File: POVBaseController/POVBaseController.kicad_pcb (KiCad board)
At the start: 2 copper layers, 53.3 x 29.2 mm, 43 parts, among them P1 CONN_01X02, P2 CONN_01X02, P3 CONN_01X05, U1 A5970AD, U2 CY8C4014LQI-412, U3 LD1117S50CTR

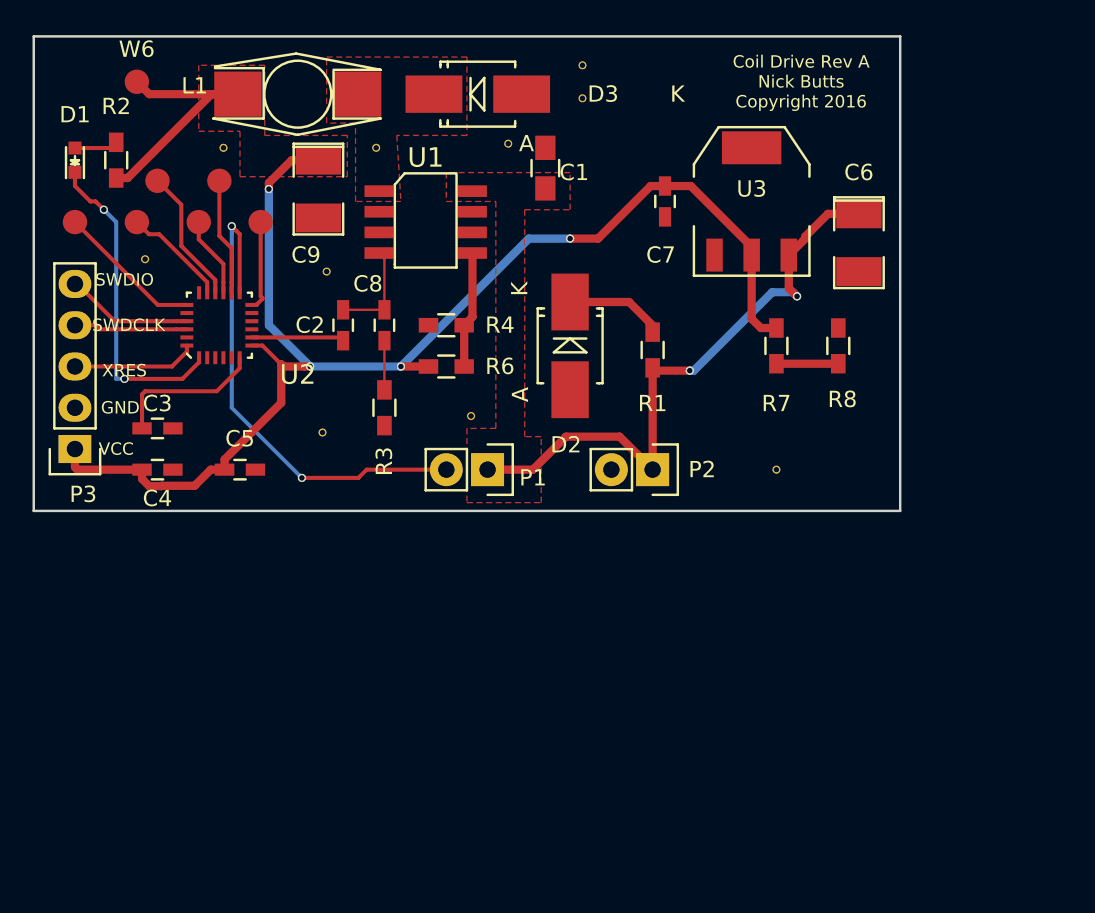
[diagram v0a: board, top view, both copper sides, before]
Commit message: Finished the POV H-Bridge controller schematic and working on layout.
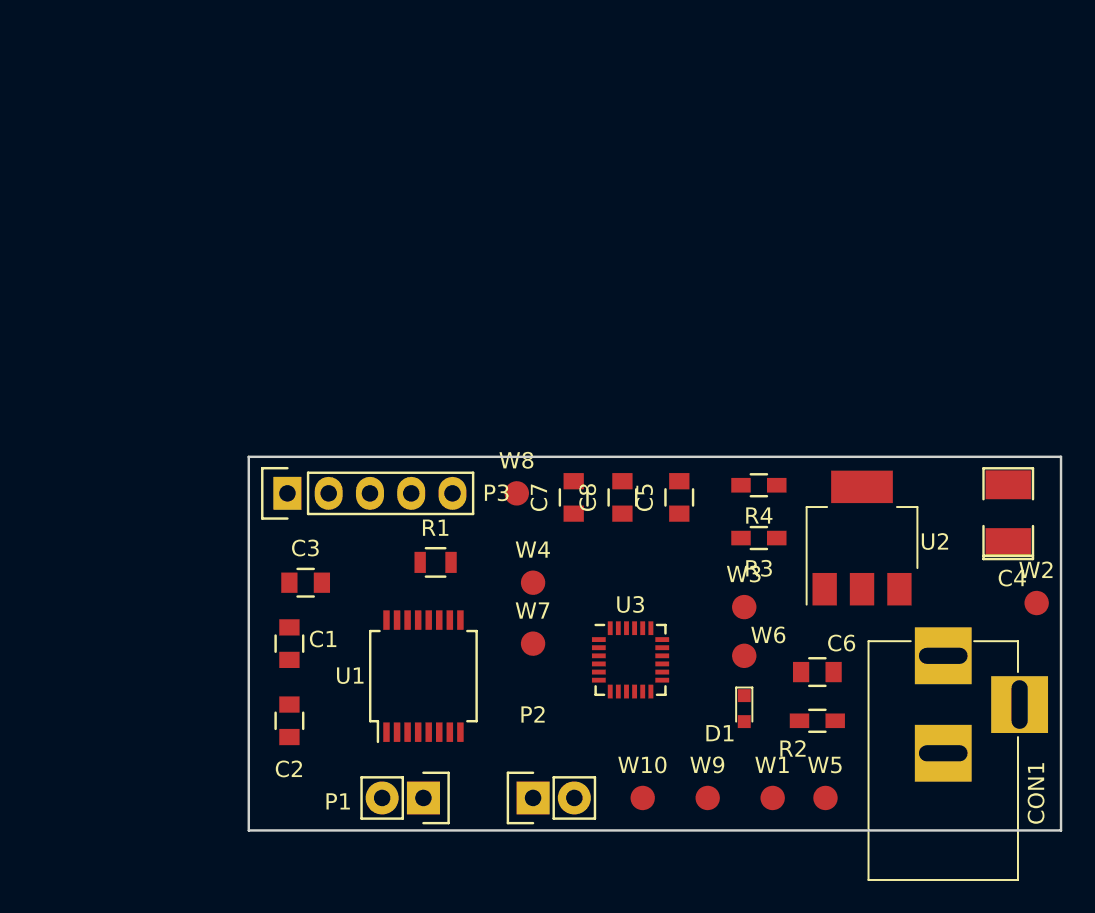
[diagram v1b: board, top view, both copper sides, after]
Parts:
- removed C9: 22u, SMD_Packages:SMD-1210_Pol
- removed D2: TVS, Diodes_SMD:SMB_Handsoldering
- removed D3: STPS2L40, Diodes_SMD:SMB_Handsoldering
- removed L1: 82u, myfootprint:TDK_Inductor_12.95x9.4x5.08
- removed R6: 13k, Resistors_SMD:R_0603_HandSoldering
- removed R7: 120, Resistors_SMD:R_0603_HandSoldering
- removed R8: 360, Resistors_SMD:R_0603_HandSoldering
- removed REF** (x10): VIA-13MILS, myfootprint:VIA-13MILS
- added CON1: BARREL_JACK, Connect:BARREL_JACK, F.Cu at (167.8, 109.2)
- added W10: RX, Measurement_Points:Measurement_Point_Round-SMD-Pad_Small, F.Cu at (149.2, 118.0)
- added W8: TEST_1P, Measurement_Points:Measurement_Point_Round-SMD-Pad_Small, F.Cu at (141.5, 99.2)
- added W9: TX, Measurement_Points:Measurement_Point_Round-SMD-Pad_Small, F.Cu at (153.2, 118.0)
- C1: value 1.5u -> 0.1u; footprint Capacitors_SMD:C_0805_HandSoldering -> Capacitors_SMD:C_0805
- C2: value 56p -> 10u; footprint Capacitors_SMD:C_0603_HandSoldering -> Capacitors_SMD:C_0805
- C3: value 0.1u -> 2.2u; footprint Capacitors_SMD:C_0603_HandSoldering -> Capacitors_SMD:C_0805
- C4: value 1u -> 10u; footprint Capacitors_SMD:C_0603_HandSoldering -> SMD_Packages:SMD-1210_Pol
- C5: footprint Capacitors_SMD:C_0603_HandSoldering -> Capacitors_SMD:C_0805
- C6: value 10u -> 100u; footprint SMD_Packages:SMD-1210_Pol -> Capacitors_SMD:C_0805
- C7: value 100u -> 1u; footprint Capacitors_SMD:C_0603_HandSoldering -> Capacitors_SMD:C_0805
- C8: value 8.2n -> 0.1u; footprint Capacitors_SMD:C_0603_HandSoldering -> Capacitors_SMD:C_0805
- R1: value 0 -> 10K; footprint Resistors_SMD:R_0603_HandSoldering -> Resistors_SMD:R_0805
- R3: value 11k -> 120
- R4: value 4.3k -> 360
- U1: value A5970AD -> DRV8848; footprint myfootprint:SO-8 -> Housings_SSOP:SSOP-16_5.3x6.2mm_Pitch0.65mm
- U2: value CY8C4014LQI-412 -> LD1117S50CTR; footprint myfootprint:QFN_24 -> TO_SOT_Packages_SMD:SOT-223
- U3: value LD1117S50CTR -> CY8C4024LQI-S401; footprint TO_SOT_Packages_SMD:SOT-223 -> Housings_DFN_QFN:QFN-24_4x4mm_Pitch0.5mm
- moved W2 60.1 mm to (173.5, 106.0)
- moved W1 55.7 mm to (157.2, 118.0)
- moved R2 55.3 mm to (160.0, 113.2), turned to 0 degrees
- moved D1 53.3 mm to (155.5, 112.5), turned to 270 degrees
- moved W5 53.2 mm to (160.5, 118.0)
- moved C4 52.4 mm to (171.8, 100.5), turned to 90 degrees
- moved W6 51.4 mm to (155.5, 109.2)
- moved W3 44.6 mm to (155.5, 106.2)
- moved U2 41.7 mm to (162.8, 102.0)
- moved C1 33.2 mm to (127.5, 108.5), turned to 270 degrees
- moved W7 30.9 mm to (142.5, 108.5)
- moved W4 30.3 mm to (142.5, 104.8)
- moved U3 29.2 mm to (148.5, 109.5)
- moved U1 28.0 mm to (135.8, 110.5), turned to 90 degrees
- moved C5 27.1 mm to (151.5, 99.5), turned to 90 degrees
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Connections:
- C1 pad 1: +12V -> GND
- C1 pad 2: GND -> +12V
- C2 pad 1: Net-(C2-Pad1) -> GND
- C2 pad 2: GND -> +12V
- C3 pad 1: Net-(C3-Pad1) -> GND
- C3 pad 2: GND -> Net-(C3-Pad2)
- C4 pad 1: VCC -> +12V
- C5 pad 1: VCC -> Net-(C5-Pad1)
- C6 pad 1: +12V -> VCC
- C8 pad 1: Net-(C2-Pad1) -> VCC
- C8 pad 2: Net-(C8-Pad2) -> GND
- P1 pad 1: +12V -> /COIL_OUT_B
- P1 pad 2: /COIL_DR -> /COIL_OUT_A
- P2 pad 1: +12V -> /MOTOR_OUT_B
- P2 pad 2: GND -> /MOTOR_OUT_A
- R1 pad 1: +12V -> VCC
- R1 pad 2: Net-(D2-Pad1) -> /nFAULT
- R3 pad 1: Net-(C8-Pad2) -> VCC
- R3 pad 2: GND -> Net-(R3-Pad2)
- R4 pad 1: Net-(R4-Pad1) -> Net-(R3-Pad2)
- U1 pad 1: Net-(D3-Pad1) -> /nSLEEP
- U1 pad 2: Net-(U1-Pad2) -> /COIL_OUT_A
- U1 pad 4: Net-(C2-Pad1) -> /COIL_OUT_B
- U1 pad 5: Net-(R4-Pad1) -> /MOTOR_OUT_B
- U1 pad 6: Net-(U1-Pad6) -> GND
- U1 pad 7: GND -> /MOTOR_OUT_A
- U1 pad 8: +12V -> /nFAULT
- U2 pad 1: /LED -> Net-(R3-Pad2)
- U2 pad 2: Net-(U2-Pad2) -> VCC
- U2 pad 3: Net-(U2-Pad3) -> +12V
- U2 pad 4: Net-(U2-Pad4) -> (no net)
- U3 pad 1: GND -> Net-(U3-Pad1)
- U3 pad 2: VCC -> /COIL_IN_A
- U3 pad 3: +12V -> /COIL_IN_B
- U3 pad 4: (no net) -> Net-(U3-Pad4)
- W1 pad 1: Net-(U2-Pad19) -> Net-(U3-Pad6)
- W2 pad 1: Net-(U2-Pad17) -> Net-(U3-Pad12)
- W3 pad 1: Net-(U2-Pad16) -> Net-(U3-Pad17)
- W4 pad 1: Net-(U2-Pad15) -> Net-(U3-Pad5)
- W5 pad 1: Net-(U2-Pad14) -> Net-(U3-Pad11)
- W6 pad 1: VCC -> Net-(U3-Pad16)
- W7 pad 1: Net-(U2-Pad12) -> Net-(U3-Pad4)
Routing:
- net VCC: track 97.3 -> 0.00 mm, vias 4 -> 0
- net +12V: track 37.6 -> 0.00 mm, vias 2 -> 0
- net /COIL_DR: track 30.7 -> 0.00 mm, vias 2 -> 0
- net /LED: track 19.8 -> 0.00 mm, vias 2 -> 0
- net GND: track 9.55 -> 0.00 mm
- net Net-(C3-Pad1): track 9.42 -> 0.00 mm
- net Net-(U2-Pad19): track 9.00 -> 0.00 mm
- net Net-(U2-Pad16): track 8.36 -> 0.00 mm
- net /SWDIO: track 7.84 -> 0.00 mm
- net /XRES: track 7.64 -> 0.00 mm
- net Net-(U2-Pad14): track 7.20 -> 0.00 mm
- net Net-(R4-Pad1): track 7.20 -> 0.00 mm
- net /SWDCLK: track 6.99 -> 0.00 mm
- net Net-(U2-Pad17): track 6.51 -> 0.00 mm
- net Net-(C2-Pad1): track 6.18 -> 0.00 mm
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- removed copper zone on F.Cu, net +12V
- removed copper zone on B.Cu, net GND
- removed copper zone on F.Cu, net GND
- removed copper zone on F.Cu, net Net-(D3-Pad1)
- removed copper zone on F.Cu, net VCC
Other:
- board size 53.3 x 29.2 mm -> 50 x 23 mm
- net class Default: via_dia 0.51 -> 0.6; via_drill 0.34 -> 0.4
- rule trace_min: 0.1524 -> 0.2
- rule via_min_size: 0.3302 -> 0.4
- board text removed: "Coil Drive Rev A Nick Butts Copyright 2016"
- board text removed: "GND"
- board text removed: "SWDCLK"
- board text removed: "SWDIO"
- board text removed: "VCC"
- board text removed: "XRES"

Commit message: Finished the layout of the POV Base Controller.
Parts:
- added REF**: via_0.3mm, KicadFootprint:via_0.3mm, F.Cu at (170.5, 105.8)
- added REF**: via_0.3mm, KicadFootprint:via_0.3mm, F.Cu at (153.5, 114.5)
- added REF**: via_0.3mm, KicadFootprint:via_0.3mm, F.Cu at (151.5, 114.5)
- added REF**: via_0.3mm, KicadFootprint:via_0.3mm, F.Cu at (152.2, 104.0)
- added REF**: via_0.3mm, KicadFootprint:via_0.3mm, F.Cu at (129.2, 101.5)
- added REF**: via_0.3mm, KicadFootprint:via_0.3mm, F.Cu at (138.0, 111.0)
- added REF**: via_0.3mm, KicadFootprint:via_0.3mm, F.Cu at (148.0, 108.8)
- added REF**: via_0.3mm, KicadFootprint:via_0.3mm, F.Cu at (144.2, 108.5)
- added REF**: via_0.3mm, KicadFootprint:via_0.3mm, F.Cu at (134.0, 102.5)
- added REF**: via_0.3mm, KicadFootprint:via_0.3mm, F.Cu at (163.0, 120.0)
- added REF**: via_0.3mm, KicadFootprint:via_0.3mm, F.Cu at (147.0, 97.0)
- added REF**: via_0.3mm, KicadFootprint:via_0.3mm, F.Cu at (168.0, 102.5)
- added REF**: via_0.3mm, KicadFootprint:via_0.3mm, F.Cu at (143.0, 97.0)
- added REF**: via_0.3mm, KicadFootprint:via_0.3mm, F.Cu at (135.0, 120.0)
- added REF**: via_0.3mm, KicadFootprint:via_0.3mm, F.Cu at (139.0, 120.0)
- added REF**: via_0.3mm, KicadFootprint:via_0.3mm, F.Cu at (143.0, 120.0)
- added REF**: via_0.3mm, KicadFootprint:via_0.3mm, F.Cu at (159.0, 120.0)
- added REF**: via_0.3mm, KicadFootprint:via_0.3mm, F.Cu at (155.0, 120.0)
- added REF**: via_0.3mm, KicadFootprint:via_0.3mm, F.Cu at (151.0, 120.0)
- added REF**: via_0.3mm, KicadFootprint:via_0.3mm, F.Cu at (147.0, 120.0)
- added REF**: via_0.3mm, KicadFootprint:via_0.3mm, F.Cu at (143.8, 102.2)
- added REF**: via_0.3mm, KicadFootprint:via_0.3mm, F.Cu at (164.5, 107.2)
- added REF**: via_0.3mm, KicadFootprint:via_0.3mm, F.Cu at (159.2, 112.2)
- added REF**: via_0.3mm, KicadFootprint:via_0.3mm, F.Cu at (158.2, 107.0)
- added REF**: via_0.3mm, KicadFootprint:via_0.3mm, F.Cu at (153.5, 98.8)
- added REF**: via_0.3mm, KicadFootprint:via_0.3mm, F.Cu at (138.2, 108.5)
- added REF**: via_0.3mm, KicadFootprint:via_0.3mm, F.Cu at (148.0, 111.5)
- added REF**: via_0.3mm, KicadFootprint:via_0.3mm, F.Cu at (149.2, 114.2)
- C6: value 100u -> 1u
- U2: value LD1117S50CTR -> LM317AEMP
- moved W1 32.7 mm to (126.5, 106.8)
- moved R2 30.4 mm to (130.2, 118.8)
- moved D1 29.0 mm to (127.0, 117.7)
- moved W9 27.0 mm to (126.5, 114.0)
- moved W5 25.3 mm to (135.2, 118.5)
- moved W10 24.0 mm to (126.5, 110.2)
- moved C3 22.8 mm to (150.5, 98.8)
- moved W6 18.7 mm to (139.2, 118.5)
- moved C1 18.6 mm to (146.0, 106.5)
- moved C2 18.5 mm to (146.0, 112.8)
- moved C5 18.2 mm to (141.2, 114.5), turned to 0 degrees
- moved W3 17.5 mm to (143.0, 118.5)
- moved W7 16.9 mm to (126.5, 103.0)
- moved U1 16.8 mm to (152.5, 109.5)
- moved P1 15.6 mm to (151.2, 116.8)
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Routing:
- net VCC: track 0.00 -> 79.6 mm, vias 0 -> 4
- net +12V: track 0.00 -> 67.2 mm, vias 0 -> 1
- net Net-(U3-Pad12): track 0.00 -> 50.5 mm, vias 0 -> 4
- net /nFAULT: track 0.00 -> 39.8 mm, vias 0 -> 3
- net /XRES: track 0.00 -> 38.5 mm, vias 0 -> 1
- net /MOTOR_IN_A: track 0.00 -> 24.1 mm, vias 0 -> 2
- net /MOTOR_IN_B: track 0.00 -> 22.0 mm, vias 0 -> 2
- net /COIL_IN_B: track 0.00 -> 21.6 mm, vias 0 -> 2
- net /nSLEEP: track 0.00 -> 19.5 mm, vias 0 -> 2
- net /COIL_IN_A: track 0.00 -> 19.0 mm, vias 0 -> 2
- net GND: track 0.00 -> 18.8 mm
- net Net-(U3-Pad5): track 0.00 -> 16.4 mm
- net Net-(C3-Pad2): track 0.00 -> 15.7 mm, vias 0 -> 2
- net Net-(U3-Pad1): track 0.00 -> 14.5 mm
- net Net-(U3-Pad11): track 0.00 -> 14.2 mm, vias 0 -> 2
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- added copper zone on B.Cu, net GND
- added copper zone on F.Cu, net GND
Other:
- net class PWR added: clearance 0.2, trace_width 0.5, via_dia 0.6, via_drill 0.4

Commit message: Order the boards.
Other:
- board text added: "POV Base Controller Rev A QNibbles LLC Copyright 2017"
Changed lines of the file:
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@@
     (area 123.252381 94.755 176.74762 123.475001)
     (thickness 1.6)
-    (drawings 4)
+    (drawings 5)
     (tracks 300)
     (zones 0)
@@
       (net 1 GND) (zone_connect 2))
   )
+  (gr_text "POV Base Controller Rev A\nQNibbles LLC\nCopyright 2017" (at 149.75 107.5) (layer B.SilkS)
+    (effects (font (size 1.5 1.5) (thickness 0.3)) (justify mirror))
+  )
   (gr_line (start 175 97) (end 175 120) (layer Edge.Cuts) (width 0.15))
